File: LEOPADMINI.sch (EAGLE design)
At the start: 47 parts, among them IC1 ATMEGA32U4-QFN

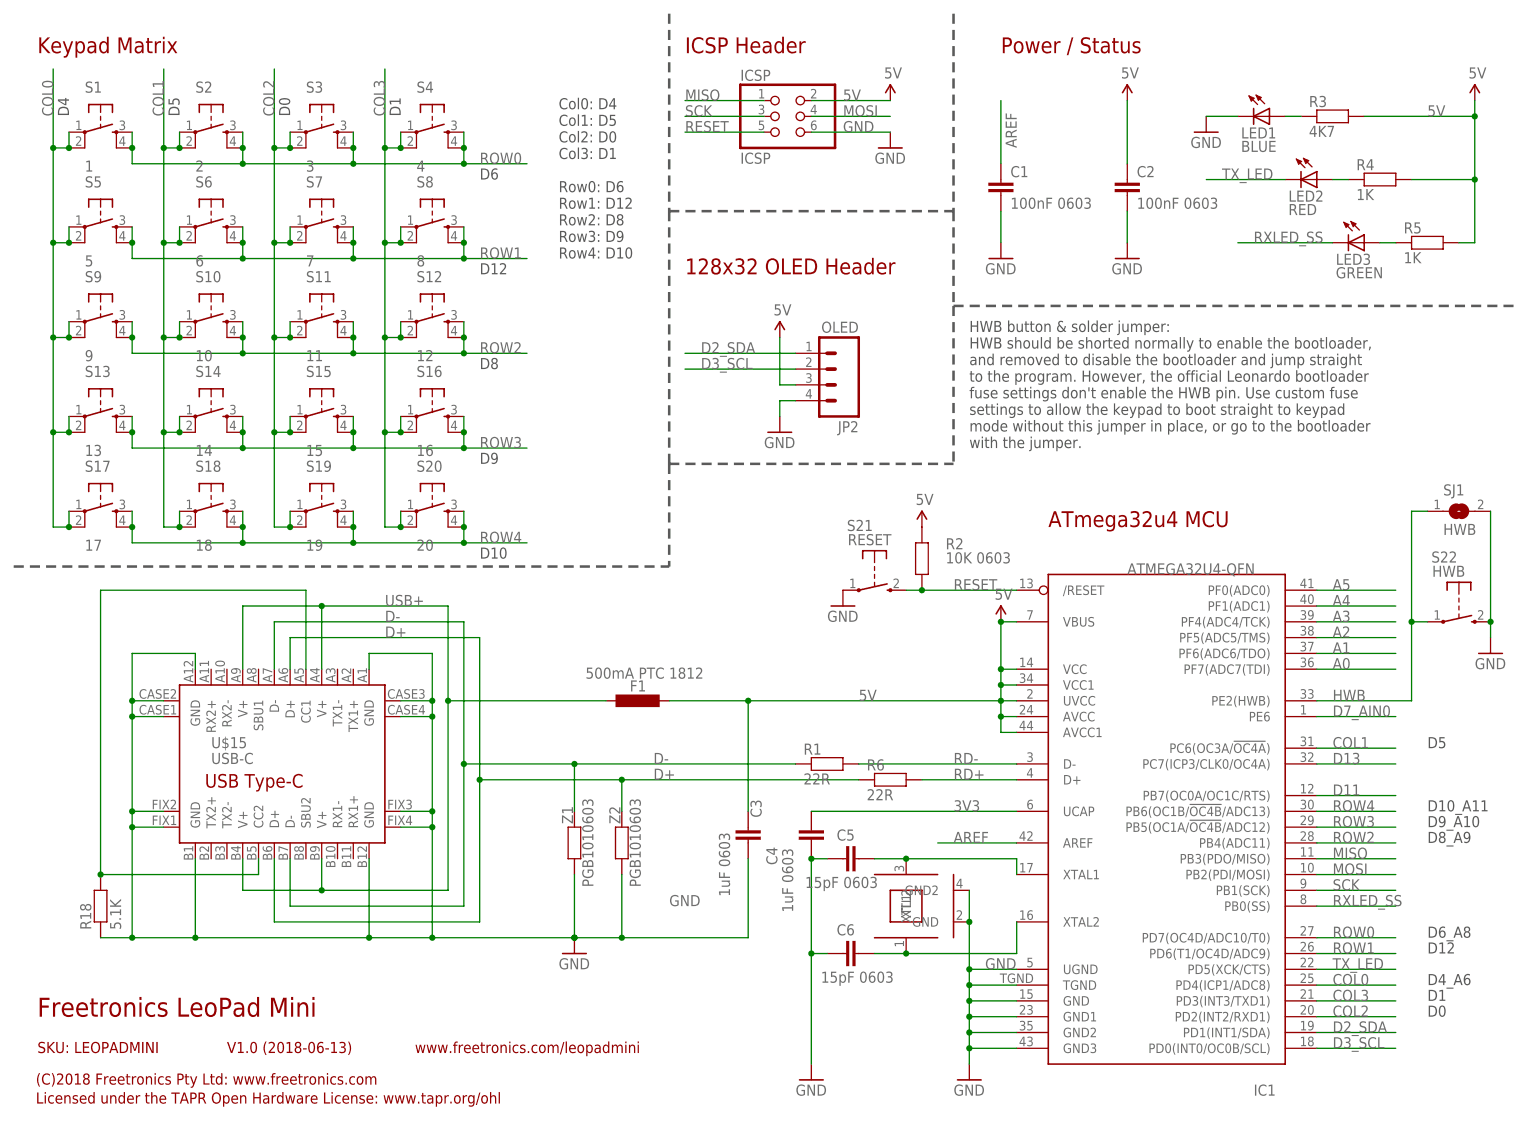
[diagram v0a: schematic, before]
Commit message: Resized to suit 6mm tact switches
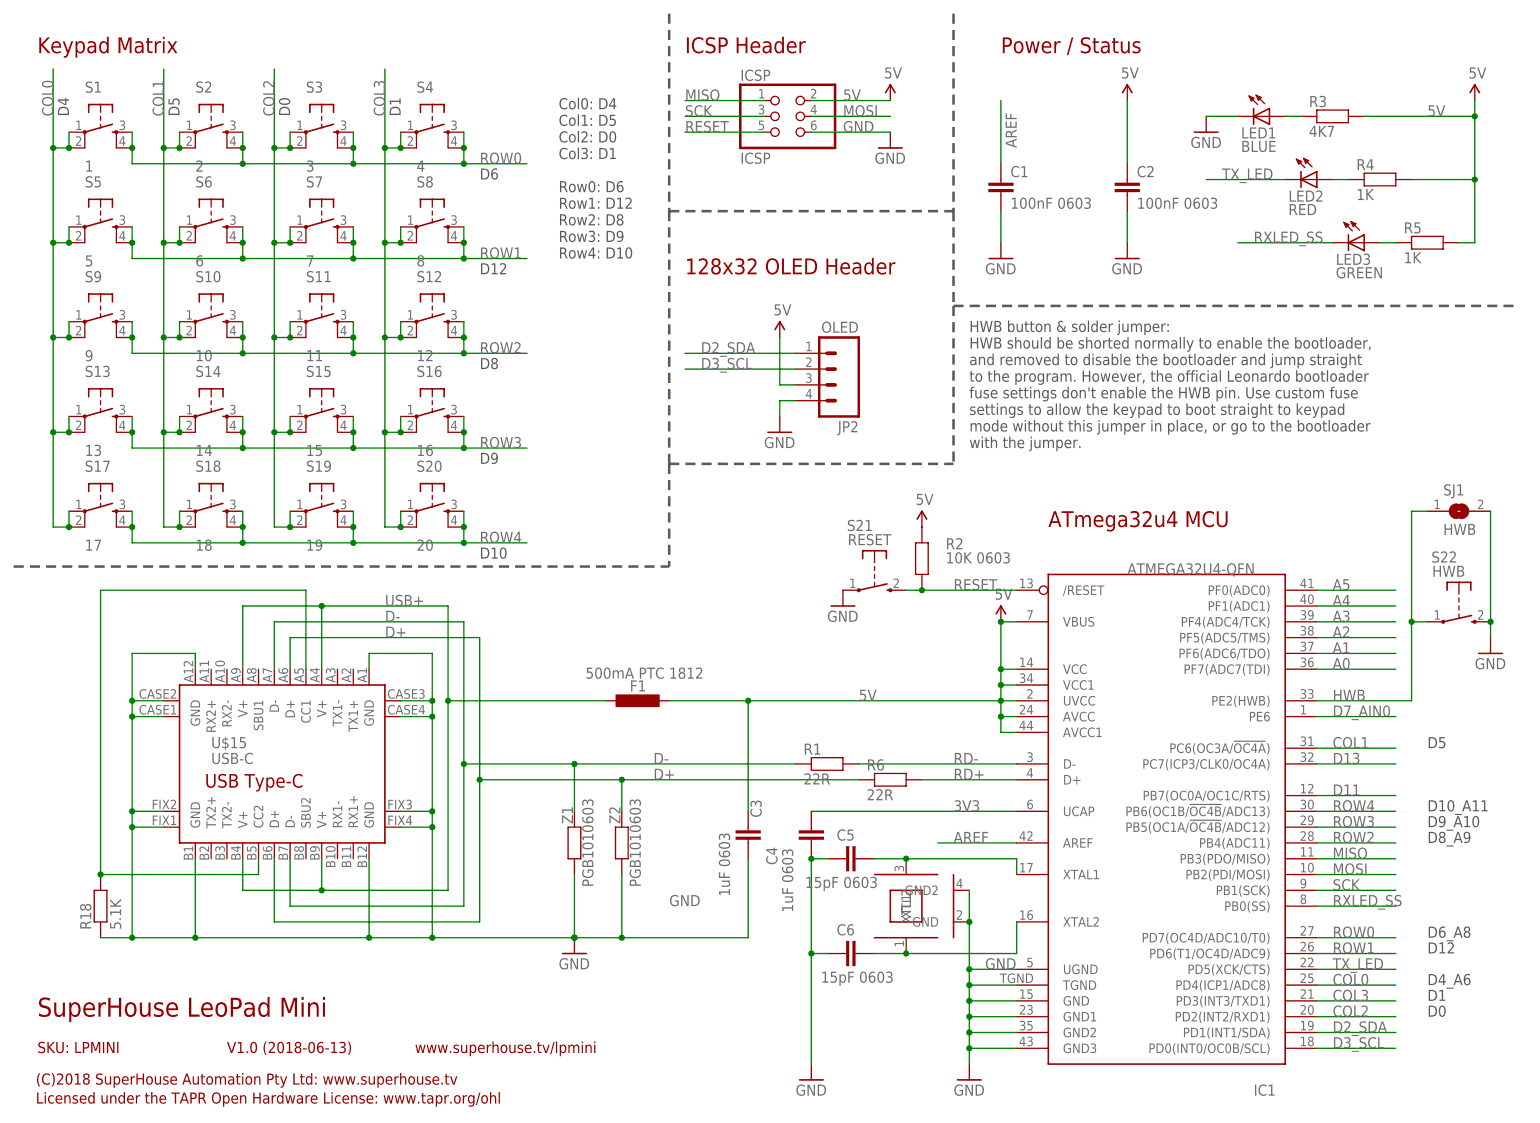
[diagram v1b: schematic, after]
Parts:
- S1, S10, S11, S12, S13, S14, S15, S16, S17, S18, S19, S2, S20, S3, S4, S5, S6, S7, S8, S9: device freetronics-jon:TAC_SWITCH4.5 -> freetronics-original:TAC_SWITCHPTH
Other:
- note added: "(C)2018 SuperHouse Automation Pty Ltd: www.superhouse.tv"
- note added: "SKU: LPMINI"
- note added: "SuperHouse LeoPad Mini"
- note added: "www.superhouse.tv/lpmini"
- note removed: "(C)2018 Freetronics Pty Ltd: www.freetronics.com"
- note removed: "Freetronics LeoPad Mini"
- note removed: "SKU: LEOPADMINI"
- note removed: "www.freetronics.com/leopadmini"
